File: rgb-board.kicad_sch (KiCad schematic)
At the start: 89 parts, among them J1 Conn_02x25_Odd_Even, J10 Conn_Coaxial, J11 Conn_Coaxial, J2 SCART-F, J3 TEST_1P, J4 TEST_1P, J5 Conn_Coaxial, J6 Conn_Coaxial, J7 Conn_Coaxial, J8 Conn_Coaxial, J9 Conn_Coaxial, Q101 BC850C, Q105 BC850C, Q109 BC850C, Q113 BC850C, Q114 BC850C, Q201 BC850C, SW1 SW_DPDT_x2, U1 NCP1117-12_SOT223

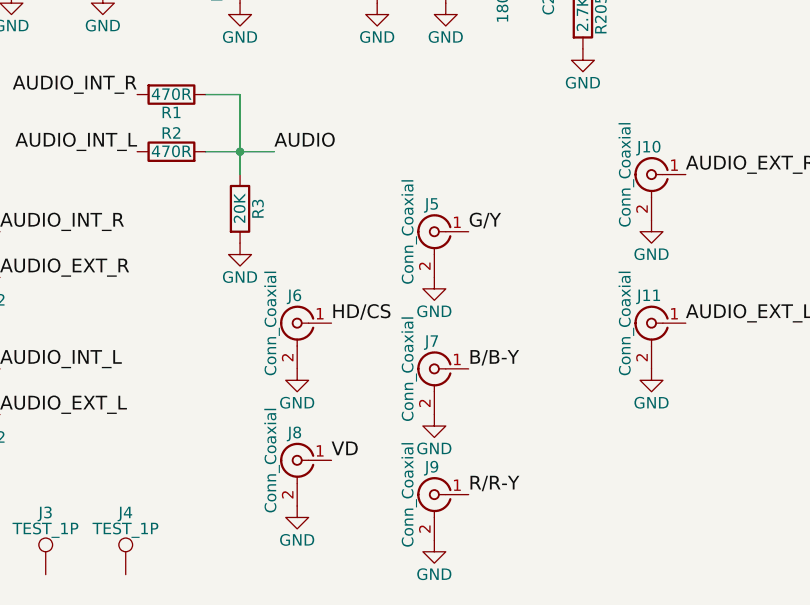
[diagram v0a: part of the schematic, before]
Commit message: Remove BNC connectors.
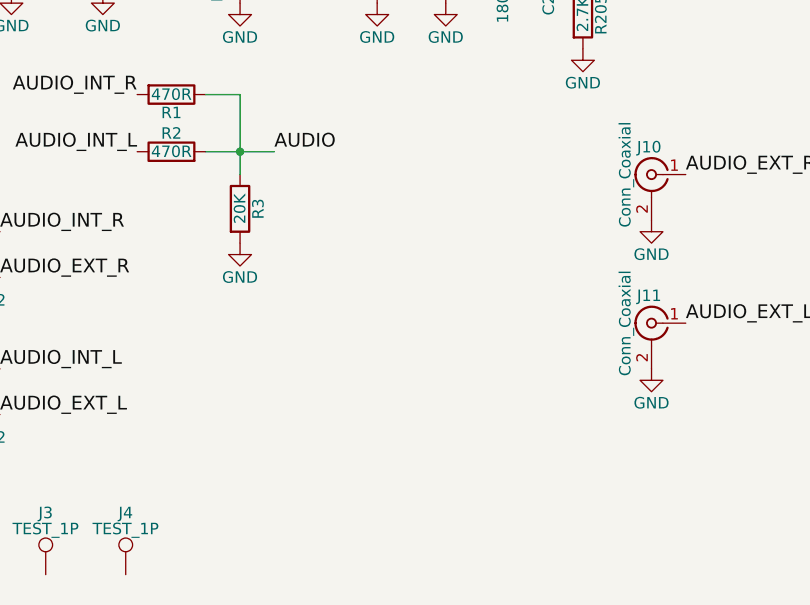
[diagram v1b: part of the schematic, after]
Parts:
- removed J5, J6, J7, J8, J9: Conn_Coaxial, bnc-tht:BNC-THT, symbol rgb-board-rescue:Conn_Coaxial-rgb-board-rescue

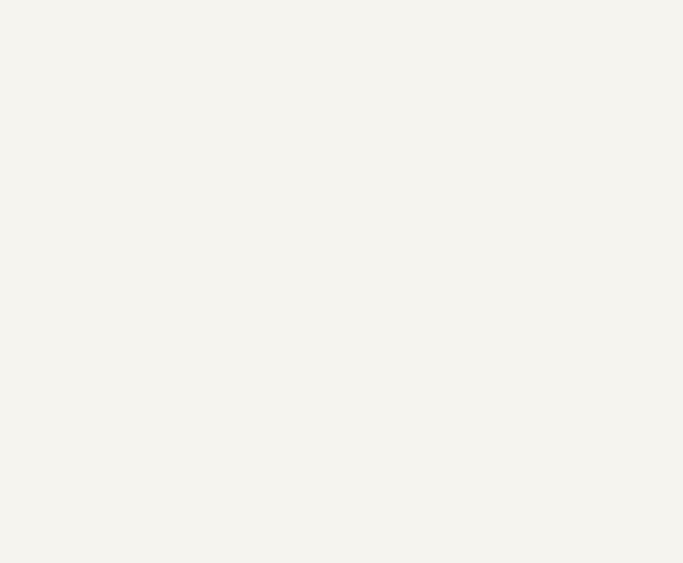
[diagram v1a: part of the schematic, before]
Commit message: Add DSUB-15 VGA Connector. Custom footprint from https://github.com/skumlos/bkm-129x-scart-vga Note pins rows spacing 2.54 mm.
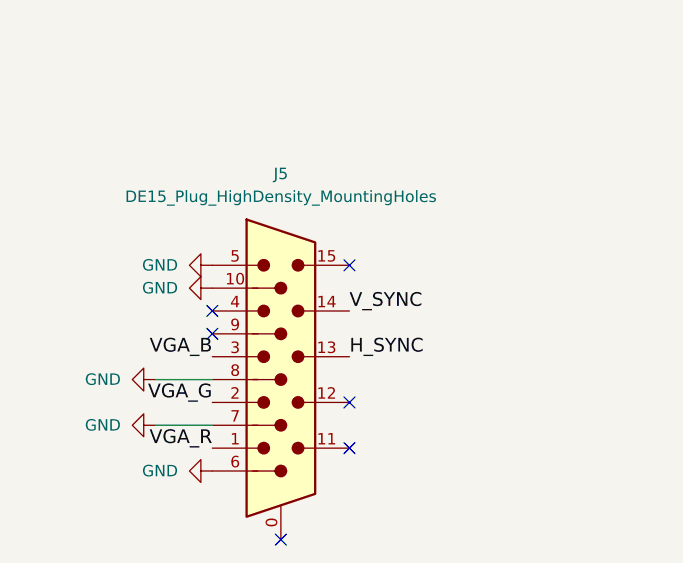
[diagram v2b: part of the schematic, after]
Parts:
- added J5: DE15_Plug_HighDensity_MountingHoles, HD15-VGA:HD15-VGA, symbol Connector:DE15_Plug_HighDensity_MountingHoles
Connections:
- net GND: now also J5.10, J5.5, J5.6, J5.7, J5.8
- new net H_SYNC: J5.13
- new net VGA_B: J5.3
- new net VGA_G: J5.2
- new net VGA_R: J5.1
- new net V_SYNC: J5.14
- no-connect marks 36 -> 42

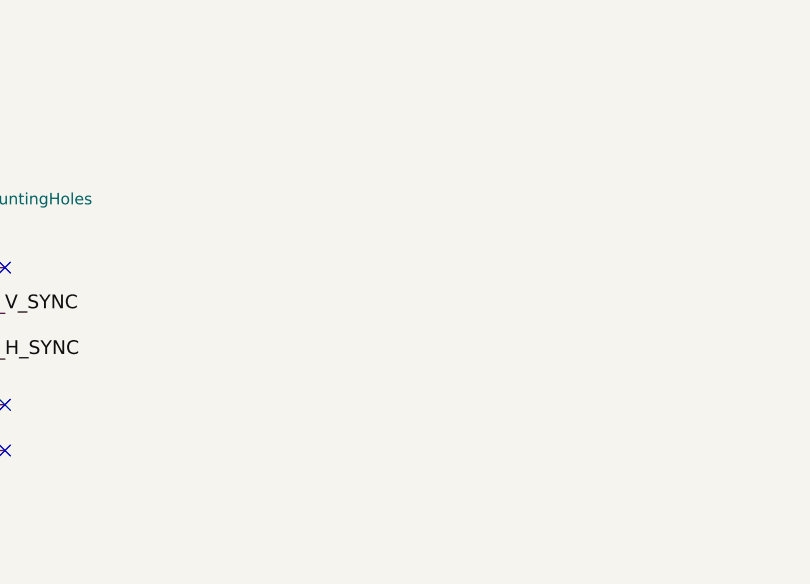
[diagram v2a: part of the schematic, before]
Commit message: Add ALPS SPUJ Series SPUJ193700 4PDT switch. Custom Push Button 4PDT symbol from https://github.com/skumlos/bkm-129x-scart-vga Custom E-Switch PBH4UEE 4PDT switch footprint from https://github.com/skumlos/bkm-129x-scart-vga
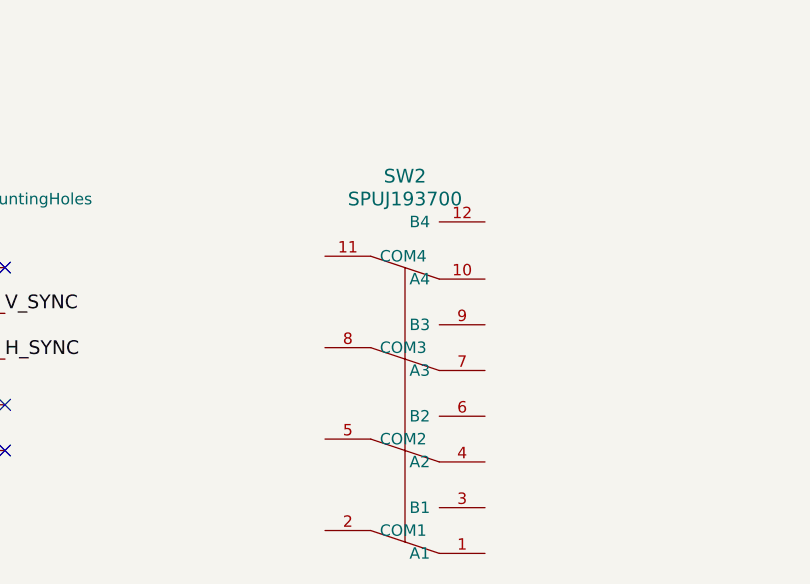
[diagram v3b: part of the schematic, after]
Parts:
- added SW2: SPUJ193700, PBH4UEE:PBH4UEE, symbol pbsw_4pdt:PBSW_4PDT
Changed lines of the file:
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@@
+	)
+	(symbol
+		(lib_id "pbsw_4pdt:PBSW_4PDT")
+		(at 95.25 234.95 90)
+		(unit 1)
+		(exclude_from_sim no)
+		(in_bom yes)
+		(on_board yes)
+		(dnp no)
+		(fields_autoplaced yes)
+		(property "Reference" "SW2"
+			(at 95.25 210.82 90)
+			(effects
+				(font
+					(size 1.524 1.524)
+				)
+			)
+		)
+		(property "Value" "SPUJ193700"
+			(at 95.25 213.36 90)
+			(effects
+				(font
+					(size 1.524 1.524)
+				)
+			)
+		)
+		(property "Footprint" "PBH4UEE:PBH4UEE"
+			(at 95.25 240.03 0)
+			(effects
+				(font
+					(size 1.524 1.524)
+				)
+				(hide yes)
+			)
+		)
+		(property "Datasheet" ""
+			(at 95.25 240.03 0)
+			(effects
+				(font
+					(size 1.524 1.524)
+				)
+				(hide yes)
+			)
+		)
+		(property "Description" "ALPS SPUJ193700"
+			(at 95.25 234.95 0)
+			(effects
+				(font
+					(size 1.27 1.27)
+				)
+				(hide yes)
+			)
+		)
+		(pin "3"
+		)
+		(pin "10"
+		)
+		(pin "9"
+		)
+		(pin "2"
+		)
+		(pin "12"
+		)
+		(pin "7"
+		)
+		(pin "6"
+		)
+		(pin "11"
+		)
+		(pin "4"
+		)
+		(pin "1"
+		)
+		(pin "5"
+		)
+		(pin "8"
+		)
+		(instances
+			(project "rgb-board"
+				(path "/fe5317b8-a5e9-4831-982f-0ff58f8d239d"
+					(reference "SW2")
+					(unit 1)
+				)
+			)
+		)
 	)
 	(symbol

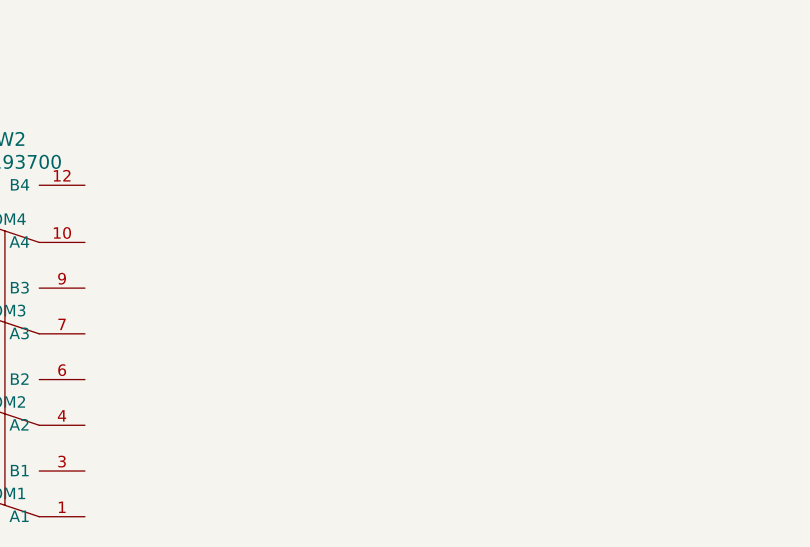
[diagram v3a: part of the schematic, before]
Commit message: Add OMRON G6K-2PY-12DC Miniature Relay Dual Pole DPDT.
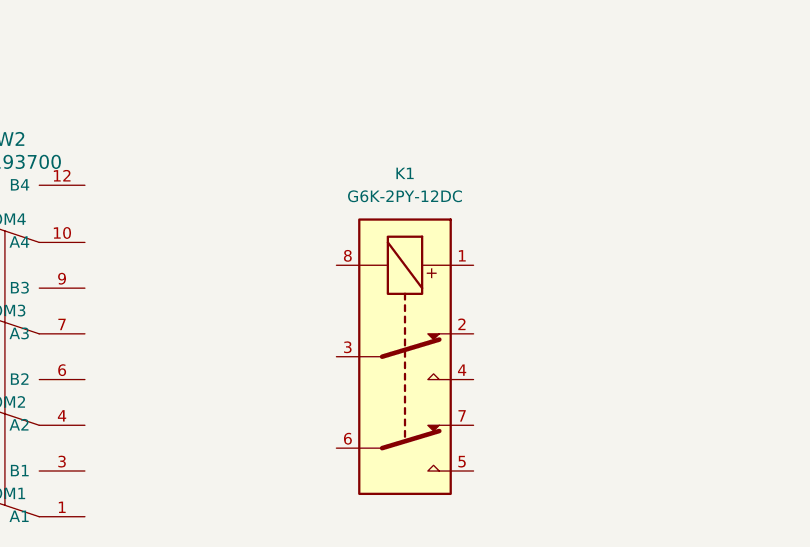
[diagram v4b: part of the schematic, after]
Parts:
- added K1: G6K-2PY-12DC, Relay_THT:Relay_DPDT_Omron_G6K-2P, symbol Relay:G6K-2
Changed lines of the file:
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@@
+	)
+	(symbol
+		(lib_id "Relay:G6K-2")
+		(at 139.7 234.95 270)
+		(unit 1)
+		(exclude_from_sim no)
+		(in_bom yes)
+		(on_board yes)
+		(dnp no)
+		(fields_autoplaced yes)
+		(property "Reference" "K1"
+			(at 139.7 214.63 90)
+			(effects
+				(font
+					(size 1.27 1.27)
+				)
+			)
+		)
+		(property "Value" "G6K-2PY-12DC"
+			(at 139.7 217.17 90)
+			(effects
+				(font
+					(size 1.27 1.27)
+				)
+			)
+		)
+		(property "Footprint" "Relay_THT:Relay_DPDT_Omron_G6K-2P"
+			(at 139.7 234.95 0)
+			(effects
+				(font
+					(size 1.27 1.27)
+				)
+				(justify left)
+				(hide yes)
+			)
+		)
+		(property "Datasheet" "http://omronfs.omron.com/en_US/ecb/products/pdf/en-g6k.pdf"
+			(at 139.7 234.95 0)
+			(effects
+				(font
+					(size 1.27 1.27)
+				)
+				(hide yes)
+			)
+		)
+		(property "Description" "Miniature 2-pole relay, Single-side Stable"
+			(at 139.7 234.95 0)
+			(effects
+				(font
+					(size 1.27 1.27)
+				)
+				(hide yes)
+			)
+		)
+		(pin "7"
+		)
+		(pin "6"
+		)
+		(pin "4"
+		)
+		(pin "5"
+		)
+		(pin "2"
+		)
+		(pin "3"
+		)
+		(pin "8"
+		)
+		(pin "1"
+		)
+		(instances
+			(project "rgb-board"
+				(path "/fe5317b8-a5e9-4831-982f-0ff58f8d239d"
+					(reference "K1")
+					(unit 1)
+				)
+			)
+		)
 	)
 	(symbol

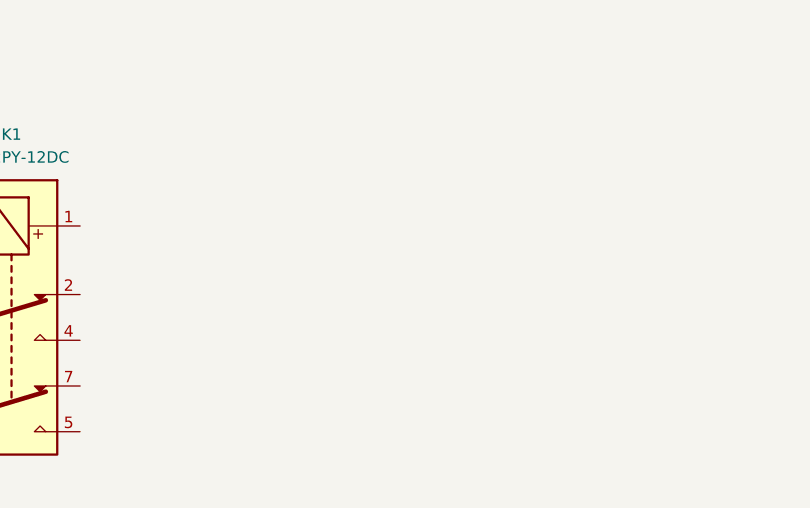
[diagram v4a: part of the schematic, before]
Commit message: Add CUI Devices / SAME SKY Devices SJ1-353XNG Series Audio Jack 3.5 mm Female.
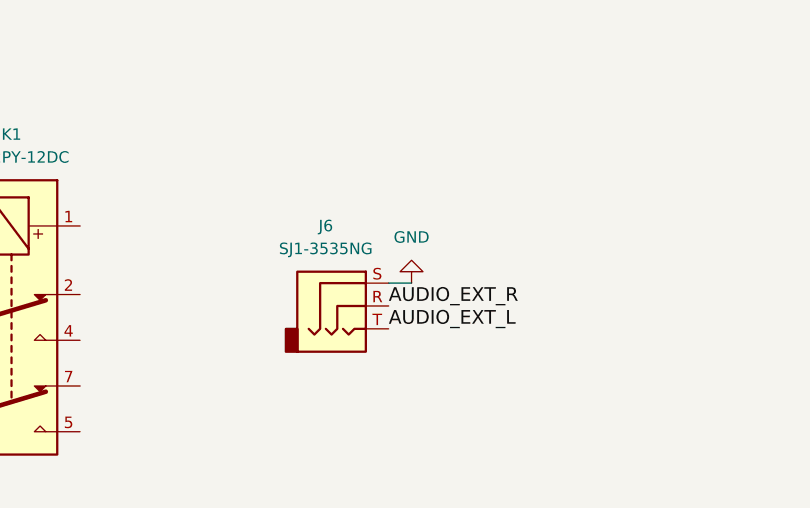
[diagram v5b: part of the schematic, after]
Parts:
- added J6: SJ1-3535NG, Connector_Audio:Jack_3.5mm_CUI_SJ1-3535NG_Horizontal, symbol Connector_Audio:AudioJack3
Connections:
- net AUDIO_EXT_L: now also J6.T
- net AUDIO_EXT_R: now also J6.R
- net GND: now also J6.S
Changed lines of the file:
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@@
 	(wire
 		(pts
+			(xy 184.15 231.14) (xy 181.61 231.14)
+		)
+		(stroke
+			(width 0)
+			(type default)
+		)
+	)
+	(wire
+		(pts
 			(xy 33.02 93.98) (xy 33.02 96.52)
 		)
@@
 		)
 	)
+	(label "AUDIO_EXT_R"
+		(at 181.61 233.68 0)
+		(fields_autoplaced yes)
+		(effects
+			(font
+				(size 1.524 1.524)
+			)
+			(justify left bottom)
+		)
+	)
 	(label "Y"
 		(at 267.97 24.13 0)
@@
 		)
 	)
+	(label "AUDIO_EXT_L"
+		(at 181.61 236.22 0)
+		(fields_autoplaced yes)
+		(effects
+			(font
+				(size 1.524 1.524)
+			)
+			(justify left bottom)
+		)
+	)
 	(label "AUDIO"
 		(at 127 143.51 0)
@@
 	)
 	(symbol
+		(lib_id "Connector_Audio:AudioJack3")
+		(at 176.53 233.68 0)
+		(unit 1)
+		(exclude_from_sim no)
+		(in_bom yes)
+		(on_board yes)
+		(dnp no)
+		(fields_autoplaced yes)
+		(property "Reference" "J6"
+			(at 174.625 224.79 0)
+			(effects
+				(font
+					(size 1.27 1.27)
+				)
+			)
+		)
+		(property "Value" "SJ1-3535NG"
+			(at 174.625 227.33 0)
+			(effects
+				(font
+					(size 1.27 1.27)
+				)
+			)
+		)
+		(property "Footprint" "Connector_Audio:Jack_3.5mm_CUI_SJ1-3535NG_Horizontal"
+			(at 176.53 233.68 0)
+			(effects
+				(font
+					(size 1.27 1.27)
+				)
+				(hide yes)
+			)
+		)
+		(property "Datasheet" "~"
+			(at 176.53 233.68 0)
+			(effects
+				(font
+					(size 1.27 1.27)
+				)
+				(hide yes)
+			)
+		)
+		(property "Description" "Audio Jack, 3 Poles (Stereo / TRS)"
+			(at 176.53 233.68 0)
+			(effects
+				(font
+					(size 1.27 1.27)
+				)
+				(hide yes)
+			)
+		)
+		(pin "T"
+		)
+		(pin "R"
+		)
+		(pin "S"
+		)
+		(instances
+			(project "rgb-board"
+				(path "/fe5317b8-a5e9-4831-982f-0ff58f8d239d"
+					(reference "J6")
+					(unit 1)
+				)
+			)
+		)
+	)
+	(symbol
 		(lib_id "power:GND")
 		(at 35.56 243.84 270)
@@
 					(unit 1)
 				)
+			)
+		)
+	)
+	(symbol
+		(lib_id "power:GND")
+		(at 184.15 231.14 180)
+		(unit 1)
+		(exclude_from_sim no)
+		(in_bom yes)
+		(on_board yes)
+		(dnp no)
+		(fields_autoplaced yes)
+		(property "Reference" "#PWR078"
+			(at 184.15 224.79 0)
+			(effects
+				(font
+					(size 1.27 1.27)
+				)
+				(hide yes)
+			)
+		)
+		(property "Value" "GND"
+			(at 184.15 226.06 0)
+			(effects
+				(font
+					(size 1.27 1.27)
+				)
+			)
+		)
+		(property "Footprint" ""
+			(at 184.15 231.14 0)
+			(effects
+				(font
+					(size 1.27 1.27)
+				)
+				(hide yes)
+			)
+		)
+		(property "Datasheet" ""
+			(at 184.15 231.14 0)
+			(effects
+				(font
+					(size 1.27 1.27)
+				)
+				(hide yes)
+			)
+		)
+		(property "Description" "Power symbol creates a global label with name \"GND\" , ground"
+			(at 184.15 231.14 0)
+			(effects
+				(font
+					(size 1.27 1.27)
+				)
+				(hide yes)
+			)
+		)
+		(pin "1"
+		)
+		(instances
+			(project "rgb-board"
+				(path "/fe5317b8-a5e9-4831-982f-0ff58f8d239d"
+					(reference "#PWR078")
+					(unit 1)
+				)

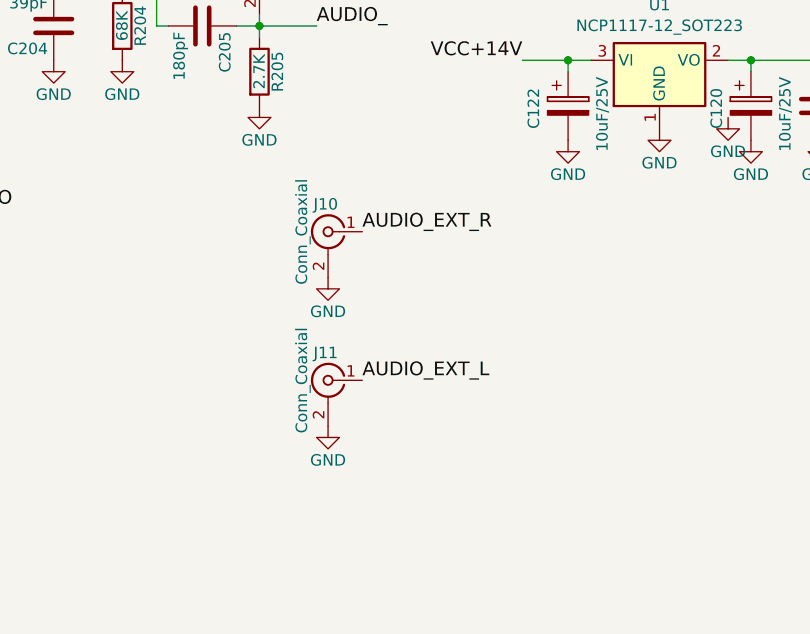
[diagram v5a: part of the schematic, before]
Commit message: Remove audio RCA connectors.
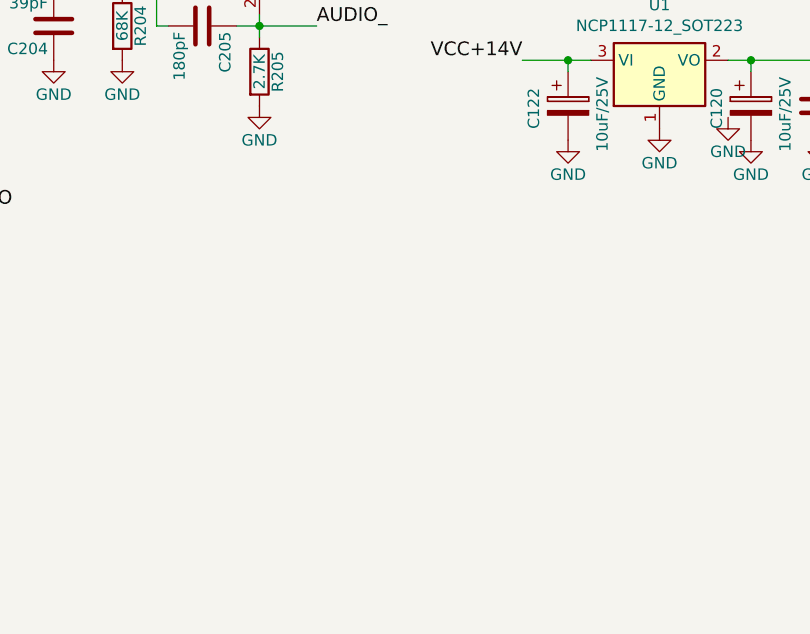
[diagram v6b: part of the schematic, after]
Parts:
- removed J10, J11: Conn_Coaxial, rcj-41x:RCJ-04X, symbol rgb-board-rescue:Conn_Coaxial-rgb-board-rescue

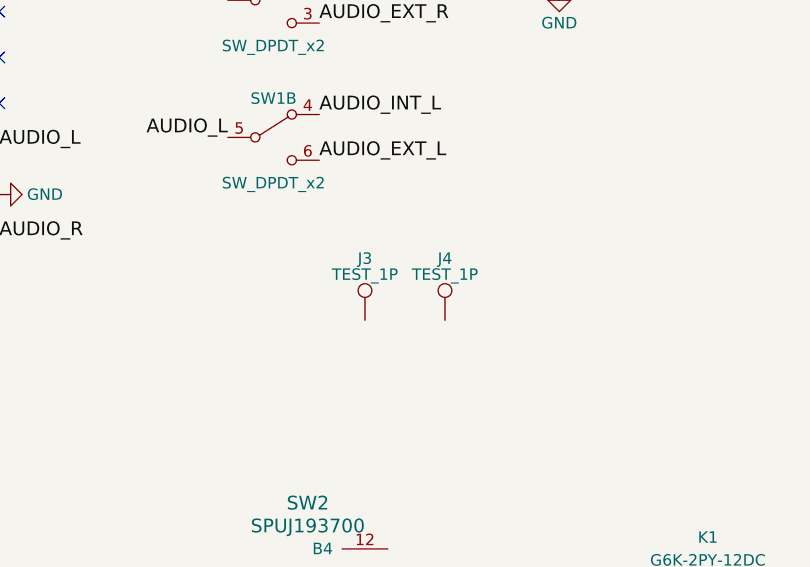
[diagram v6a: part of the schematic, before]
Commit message: Delete mounting holes / test points.
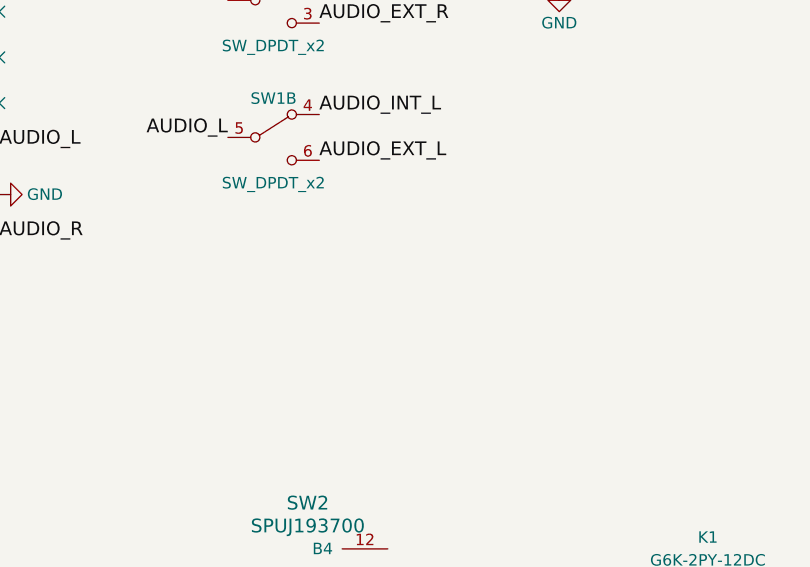
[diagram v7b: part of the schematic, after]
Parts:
- removed J3, J4: TEST_1P, Mounting_Holes:MountingHole_3.2mm_M3, symbol rgb-board-rescue:TEST_1P-rgb-board-rescue
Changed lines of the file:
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@@
-	)
-	(symbol
-		(lib_id "rgb-board-rescue:TEST_1P-rgb-board-rescue")
-		(at 101.6 190.5 0)
-		(unit 1)
-		(exclude_from_sim no)
-		(in_bom yes)
-		(on_board yes)
-		(dnp no)
-		(property "Reference" "J3"
-			(at 101.6 183.642 0)
-			(effects
-				(font
-					(size 1.27 1.27)
-				)
-			)
-		)
-		(property "Value" "TEST_1P"
-			(at 101.6 185.42 0)
-			(effects
-				(font
-					(size 1.27 1.27)
-				)
-			)
-		)
-		(property "Footprint" "Mounting_Holes:MountingHole_3.2mm_M3"
-			(at 106.68 190.5 0)
-			(effects
-				(font
-					(size 1.27 1.27)
-				)
-				(hide yes)
-			)
-		)
-		(property "Datasheet" ""
-			(at 106.68 190.5 0)
-			(effects
-				(font
-					(size 1.27 1.27)
-				)
-				(hide yes)
-			)
-		)
-		(property "Description" ""
-			(at 101.6 190.5 0)
-			(effects
-				(font
-					(size 1.27 1.27)
-				)
-				(hide yes)
-			)
-		)
-		(pin "1"
-		)
-		(instances
-			(project "rgb-board"
-				(path "/fe5317b8-a5e9-4831-982f-0ff58f8d239d"
-					(reference "J3")
-					(unit 1)
-				)
-			)
-		)
-	)
-	(symbol
-		(lib_id "rgb-board-rescue:TEST_1P-rgb-board-rescue")
-		(at 110.49 190.5 0)
-		(unit 1)
-		(exclude_from_sim no)
-		(in_bom yes)
-		(on_board yes)
-		(dnp no)
-		(property "Reference" "J4"
-			(at 110.49 183.642 0)
-			(effects
-				(font
-					(size 1.27 1.27)
-				)
-			)
-		)
-		(property "Value" "TEST_1P"
-			(at 110.49 185.42 0)
-			(effects
-				(font
-					(size 1.27 1.27)
-				)
-			)
-		)
-		(property "Footprint" "Mounting_Holes:MountingHole_3.2mm_M3"
-			(at 115.57 190.5 0)
-			(effects
-				(font
-					(size 1.27 1.27)
-				)
-				(hide yes)
-			)
-		)
-		(property "Datasheet" ""
-			(at 115.57 190.5 0)
-			(effects
-				(font
-					(size 1.27 1.27)
-				)
-				(hide yes)
-			)
-		)
-		(property "Description" ""
-			(at 110.49 190.5 0)
-			(effects
-				(font
-					(size 1.27 1.27)
-				)
-				(hide yes)
-			)
-		)
-		(pin "1"
-		)
-		(instances
-			(project "rgb-board"
-				(path "/fe5317b8-a5e9-4831-982f-0ff58f8d239d"
-					(reference "J4")
-					(unit 1)
-				)
-			)
-		)
 	)
 	(symbol
